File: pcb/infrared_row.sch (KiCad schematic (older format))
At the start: 16 parts, among them U2 CD4051B

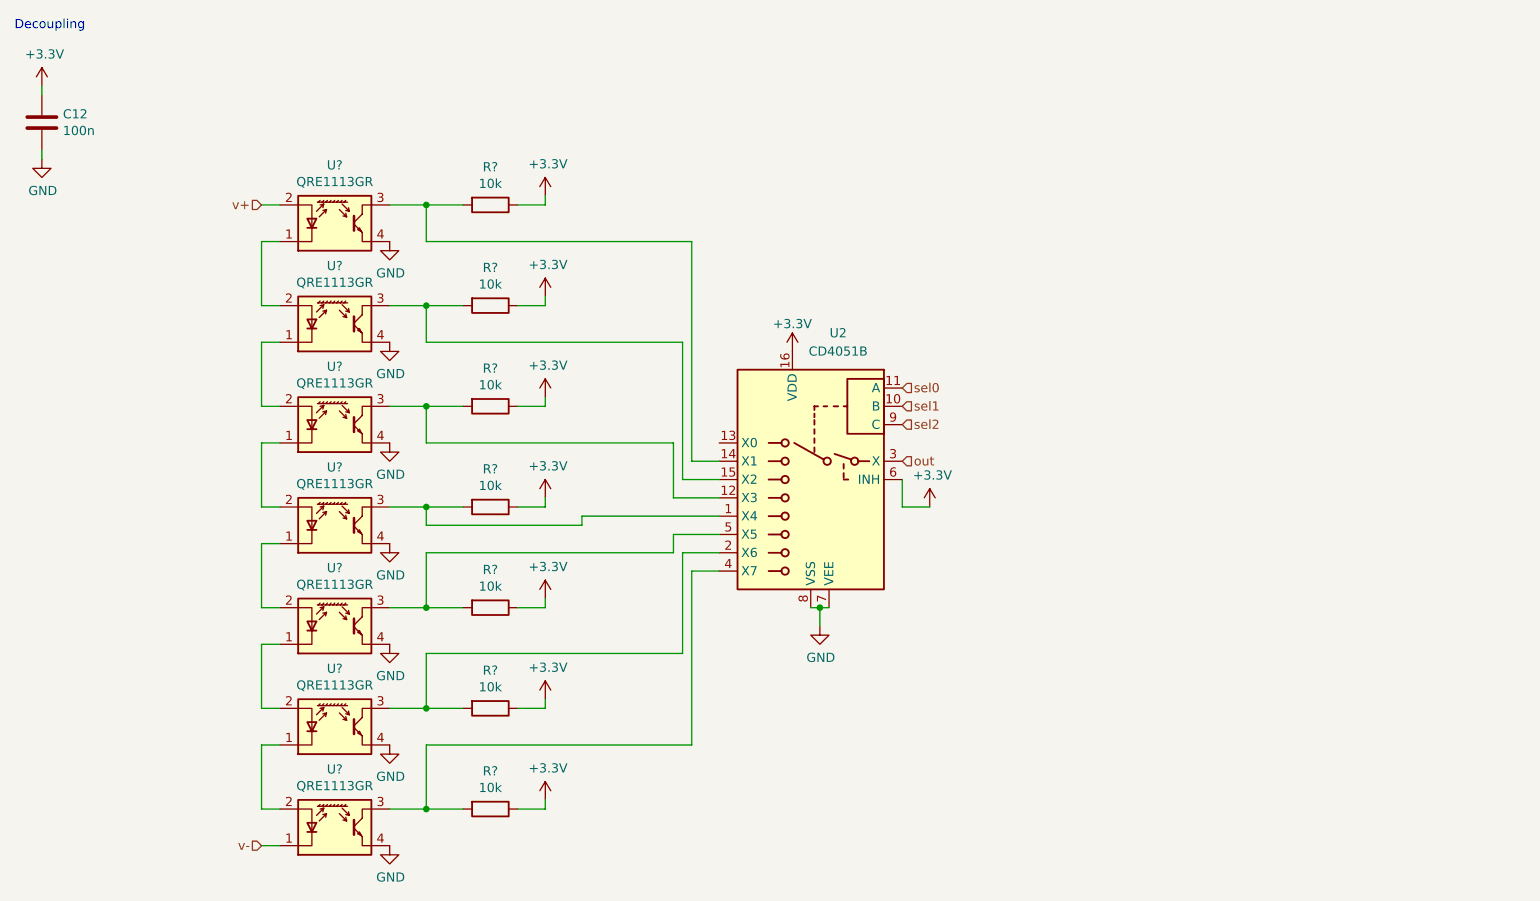
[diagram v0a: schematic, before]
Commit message: IR Matrix - Missing Supply Connection
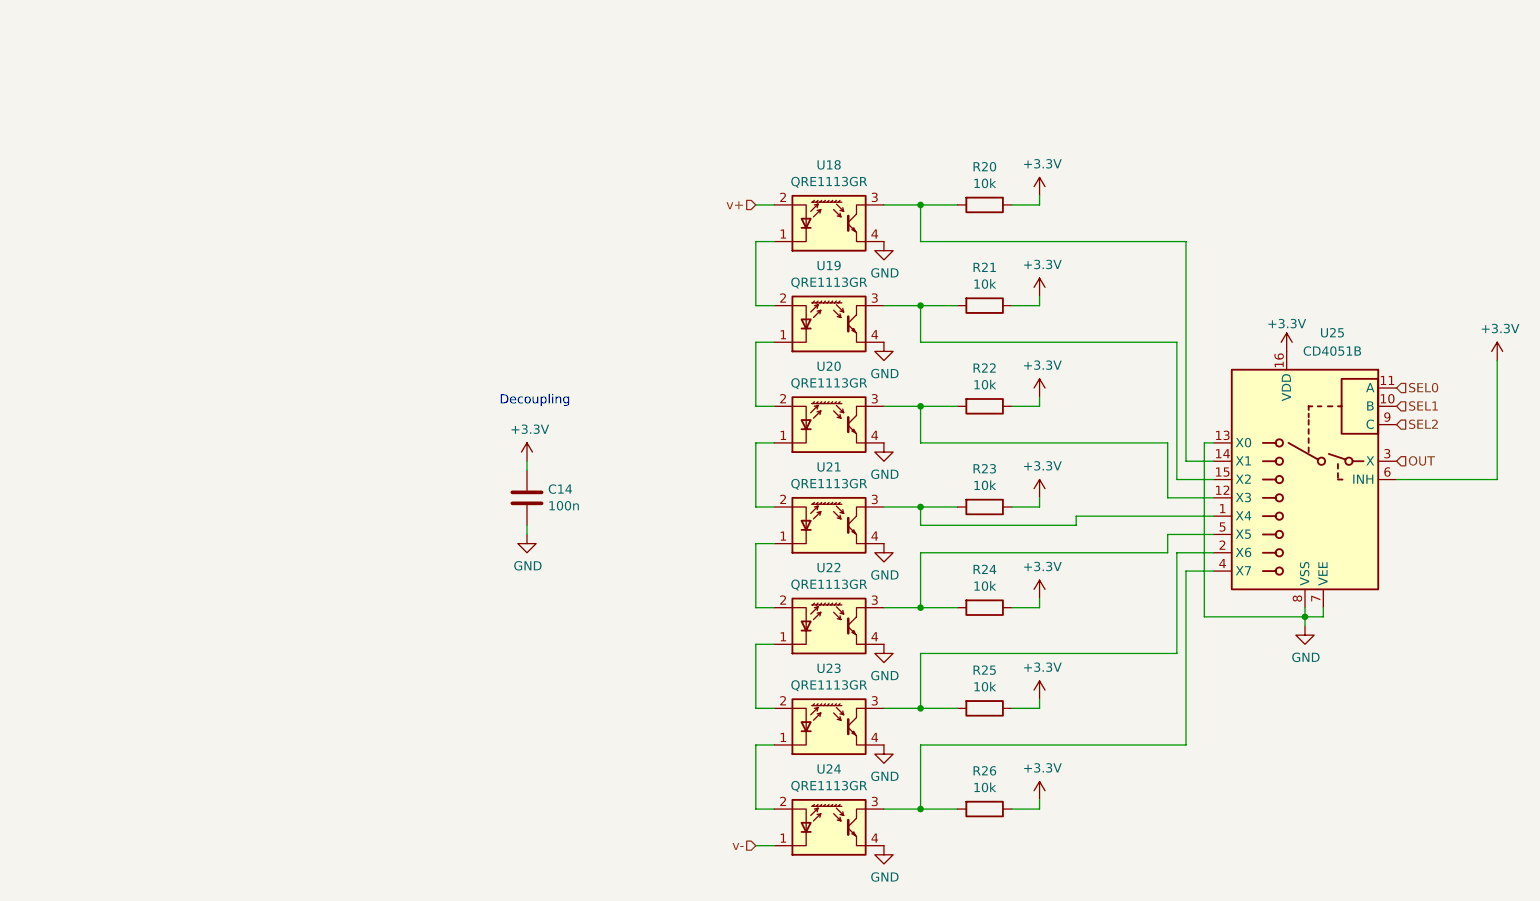
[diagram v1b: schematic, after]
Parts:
- gave numbers to parts that had none: 14
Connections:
- net GND: now also U2.13 (X0)
- net out renamed OUT
- net sel0 renamed SEL0
- net sel1 renamed SEL1
- net sel2 renamed SEL2
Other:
- moved on the sheet: C14, R20, R21, R22, R23, R24, R25, R26, U18, U19, U20, U21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

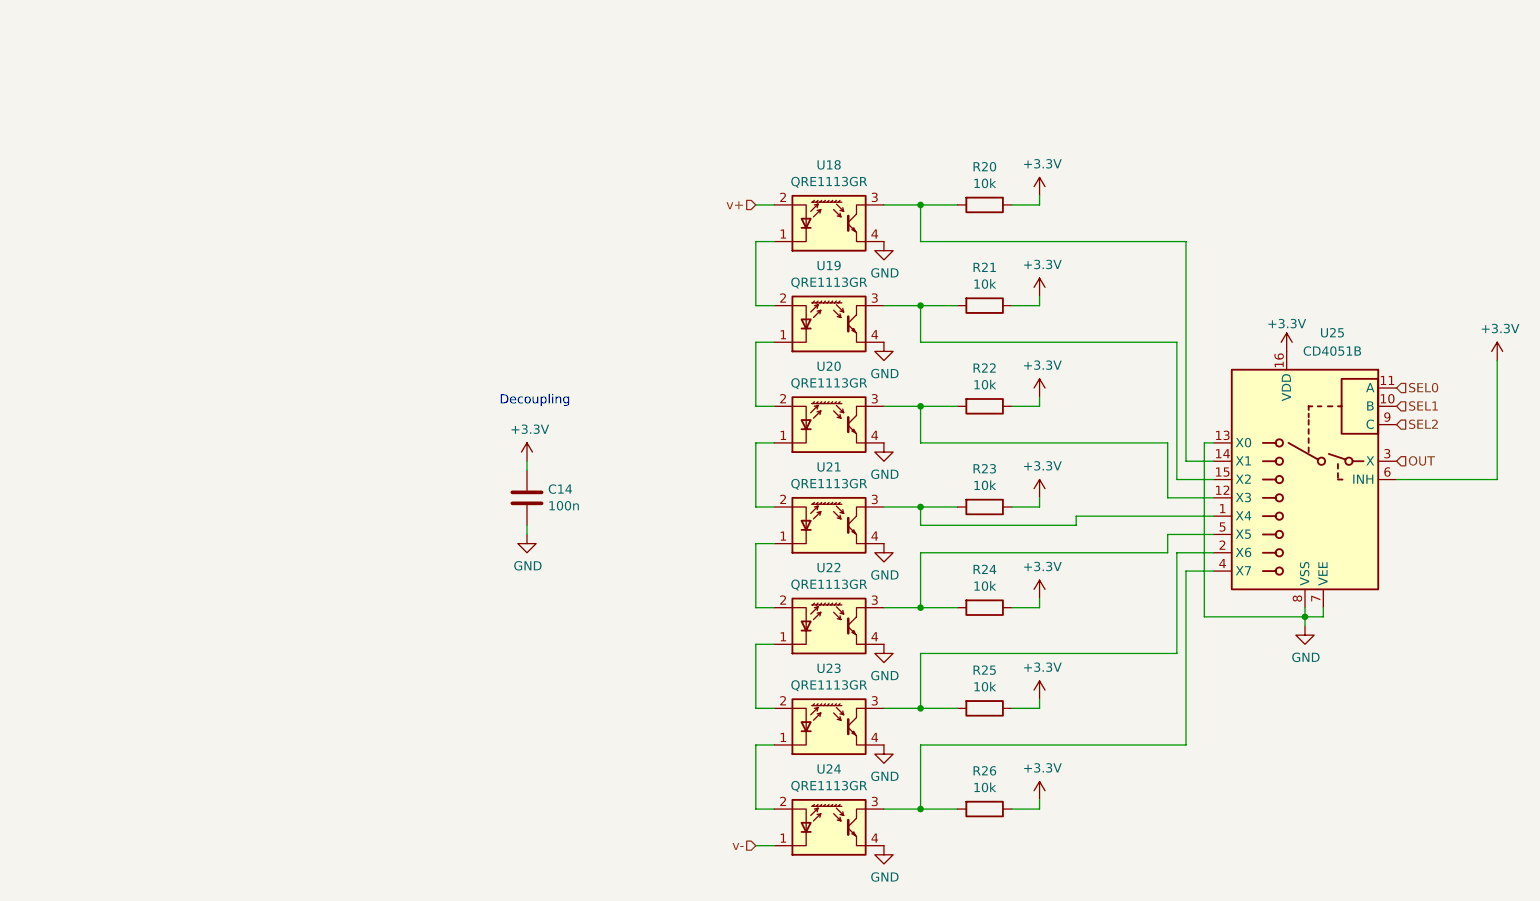
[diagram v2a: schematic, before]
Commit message: Fix IR Sensors
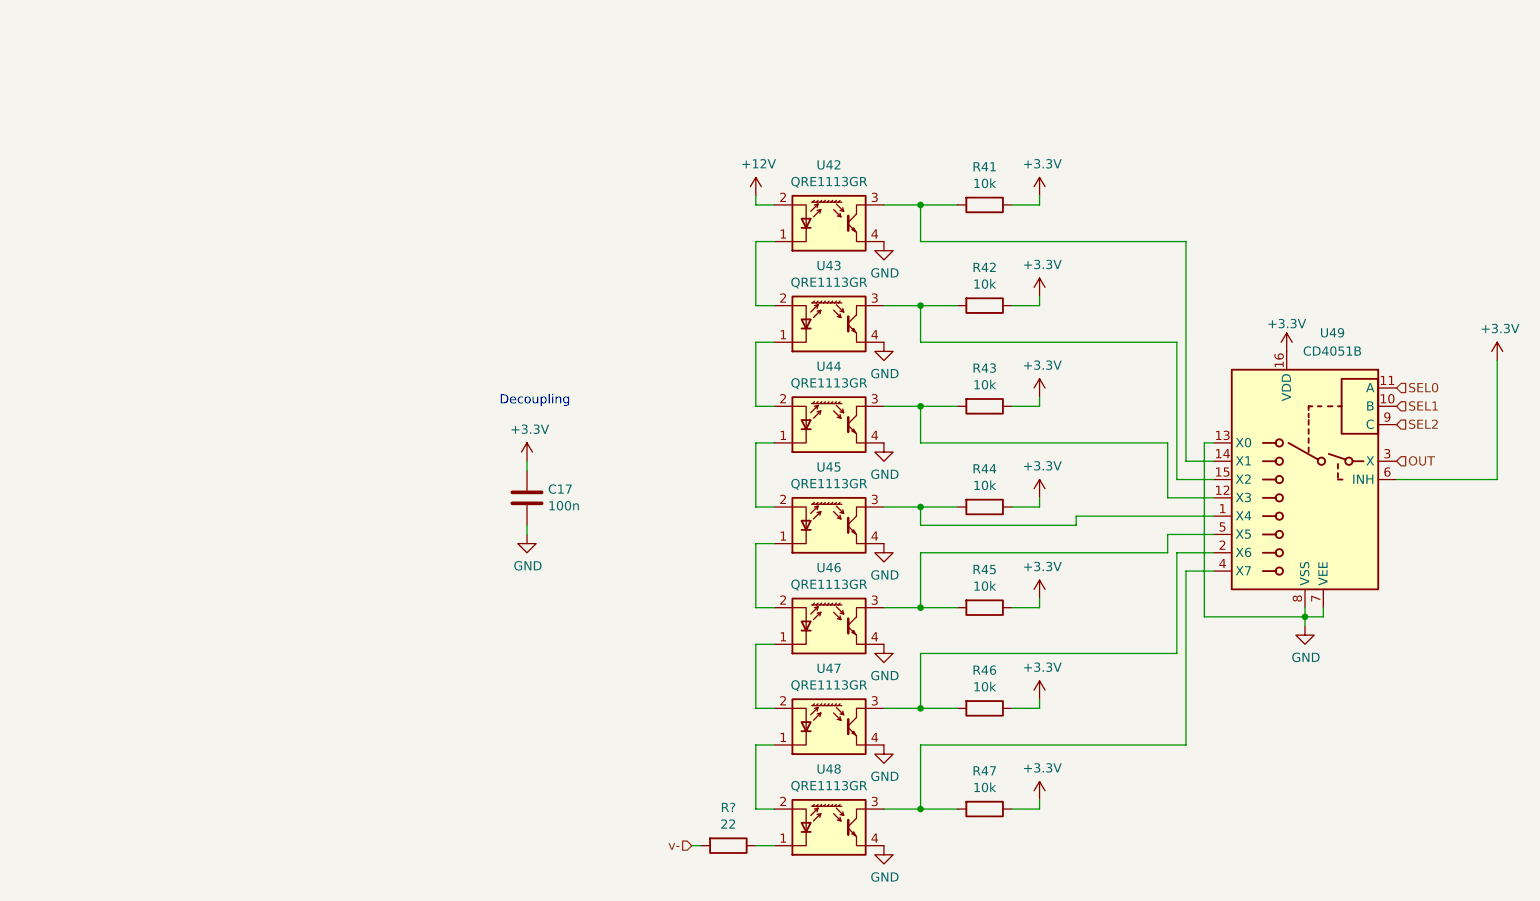
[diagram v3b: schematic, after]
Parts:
- added R?: 22, symbol Device:R
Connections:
- net v-: now also R?.2; no longer U9.1 (K)
- net v+ renamed +12V
- new net: R?.1, U9.1 (K)

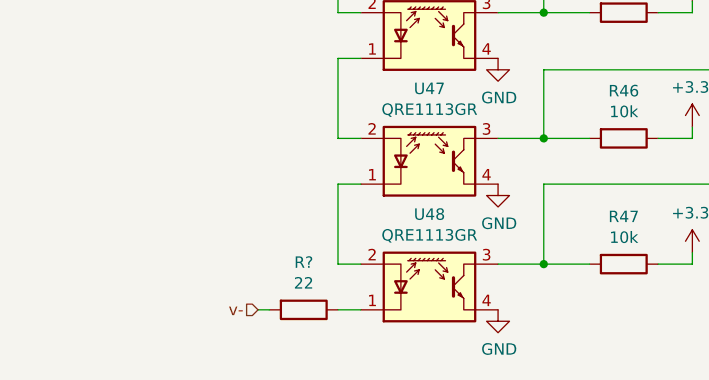
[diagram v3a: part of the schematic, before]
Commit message: Fix resistor IR Matrix
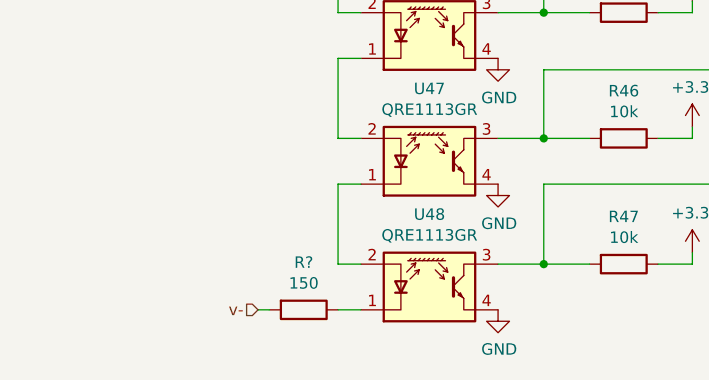
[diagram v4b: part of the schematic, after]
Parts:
- R?: value 22 -> 150
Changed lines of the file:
@@
 $Descr A4 11693 8268
 encoding utf-8
-Sheet 10 12
+Sheet 11 12
 Title ""
 Date ""
@@
 U 1 1 5D3F2415
 P 4950 5550
+AR Path="/5D1373A3/5D25183D/5D40E002/5D3F2415" Ref="R?"  Part="1"
+AR Path="/5D1373A3/5D25183D/5D40DB29/5D3F2415" Ref="R?"  Part="1"
+AR Path="/5D1373A3/5D25183D/5D40DD62/5D3F2415" Ref="R?"  Part="1"
+AR Path="/5D1373A3/5D25183D/5D254F86/5D3F2415" Ref="R?"  Part="1"
+AR Path="/5D1373A3/5D25183D/5D40D6FB/5D3F2415" Ref="R?"  Part="1"
+AR Path="/5D1373A3/5D25183D/5D40DA1E/5D3F2415" Ref="R?"  Part="1"
+AR Path="/5D1373A3/5D25183D/5D40DC5E/5D3F2415" Ref="R?"  Part="1"
 F 0 "R?" V 4743 5550 50  0000 C CNN
-F 1 "22" V 4834 5550 50  0000 C CNN
+F 1 "150" V 4834 5550 50  0000 C CNN
 F 2 "" V 4880 5550 50  0001 C CNN
 F 3 "~" H 4950 5550 50  0001 C CNN
@@
 U 1 1 5D3F7858
 P 5100 2000
+AR Path="/5D1373A3/5D25183D/5D40E002/5D3F7858" Ref="#PWR?"  Part="1"
+AR Path="/5D1373A3/5D25183D/5D40DB29/5D3F7858" Ref="#PWR?"  Part="1"
+AR Path="/5D1373A3/5D25183D/5D40DD62/5D3F7858" Ref="#PWR?"  Part="1"
 F 0 "#PWR?" H 5100 1850 50  0001 C CNN
 F 1 "+12V" H 5115 2173 50  0000 C CNN
